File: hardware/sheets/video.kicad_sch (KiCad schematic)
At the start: 41 parts, among them J1 HDMI_A, J2 VGA HD15, M1 Core2350B (8MB PSRAM), U2 74LVC245A, U3 74LVC245A, U4 74LVC245A, U5 74LVC245A

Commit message: Passives: basic-library audit + 4x resistor-array pull consolidation
Audit: every discrete R/C value was already JLC basic except the ferrite
beads -- swapped to basic Murata BLM18PG121SN1D (C14709, 120R@100MHz,
same family/role). The 100uF electrolytic and buck inductor stay
extended (zero fee-free parts exist in those subcategories). Pruned the
orphaned 5V-era 47nF/330nF MAX3241 cap entries.

Pull consolidation: 65 discrete 10k/4.7k rail pulls across 8 sheets
collapse into 18 basic 4-element isolated arrays (4D03WGJ0103T5E /
4D03WGJ0472T5E, element k = pins k/9-k; new mxbus.r_pack4 helper).
Isolated elements let packs mix rails; every net keeps its exact rail
and semantics (verified element-by-element in the netlist). RC/divider/
series/I2C resistors stay discrete. Board 452 -> 406 components; also
de-risks the sole basic 10k 0603 line (0 stock at audit). Audit
recorded in jlcpcb-sourcing.md.

Co-Authored-By: Claude Fable 5 <noreply@anthropic.com>
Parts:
- removed JP1: VID_BASE, Connector_PinHeader_2.54mm:PinHeader_1x02_P2.54mm_Vertical, symbol Connector_Generic:Conn_01x02
- removed R33, R34, R35, R36: 10k, Resistor_SMD:R_0603_1608Metric, symbol Device:R
- added RN2: 10kx4, Resistor_SMD:R_Array_Convex_4x0603, symbol Device:R_Pack04
- JP1: renamed from R31; value 10k -> VID_BASE; footprint Resistor_SMD:R_0603_1608Metric -> Connector_PinHeader_2.54mm:PinHeader_1x02_P2.54mm_Vertical; symbol Device:R -> Connector_Generic:Conn_01x02; LCSC Part Num C25804 -> C2337
- RN1: renamed from R32; value 10k -> 10kx4; footprint Resistor_SMD:R_0603_1608Metric -> Resistor_SMD:R_Array_Convex_4x0603; symbol Device:R -> Device:R_Pack04; LCSC Part Num C25804 -> C29718
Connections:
- net 3V3_VID: now also RN1.5 (R4.2), RN1.6 (R3.2), RN1.7 (R2.2), RN1.8 (R1.2), RN2.8 (R1.2); no longer JP1.1
- net AOE_HI: now also RN1.4 (R4.1)
- net AOE_LO: now also RN1.2 (R2.1)
- net AOE_MID: now also RN1.3 (R3.1)
- net DDIR: now also RN2.2 (R2.1); no longer RN1.2
- net DOE: now also RN1.1 (R1.1)
- net GND: now also JP1.2 (Pin_2), RN2.7 (R2.2); no longer RN1.1
- net VID_BASE: now also JP1.1 (Pin_1), RN2.1 (R1.1); no longer JP1.2
- no-connect marks 30 -> 34

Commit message: Remove the on-board RTL8019AS NIC (tag full-board-with-nic preserves it)
Network sheet, symbols, and NIC-only parts.py bindings deleted; addr_decode
JP6->JP5 (DIS_VID); IRQ2 retired as an internal net like IRQ6/IRQ8 (still
reachable as EXT_IRQ2 from the expansion port). ERC stays 0/0.

Co-Authored-By: Claude Fable 5 <noreply@anthropic.com>
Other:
- note added: "SOFT CARD: ISA bus + power ONLY. Self-decodes 0xA0000-0xBFFFF and 3B4/3B5/3B8/3BA/3BF + 3D4/3D5/3D8/3D9/3DA from snooped A17-A19/A0-A9. No Y5, no link, no host RAM (design S8). Disable: addr_decode JP5 (DIS_VID high, firmware keeps all OEs off; enabled by default). JP1 = CGA (closed) / MDA (open) window set."
- note removed: "SOFT CARD: ISA bus + power ONLY. Self-decodes 0xA0000-0xBFFFF and 3B4/3B5/3B8/3BA/3BF + 3D4/3D5/3D8/3D9/3DA from snooped A17-A19/A0-A9. No Y5, no link, no host RAM (design S8). Disable: addr_decode JP6 (DIS_VID high, firmware keeps all OEs off; enabled by default). JP1 = CGA (closed) / MDA (open) window set."

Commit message: Expansion port: 50-pin header, port DMA channel, dev cards deleted
Two waves of the 2026-07-14/15 expansion-port rework (the first was
uncommitted): the IRQ-scan collapse to one '165 + '32 OR rank with
ISA-card DMA removed outright, then the port redesign that brings one
DMA channel back:

- isa_conn: 60-pin (2x30, PicoGUS-standard layout) -> 50-pin (2x25,
  project-private pinout; 50-way IDC is far easier to source). OSC and
  ~REFRESH dropped to fit (no on-board consumer / no DRAM refresh; the
  planned ISA backplane board re-creates both for period cards).
- Port DMA: EXT_DRQ rides the sidecar inbound '244 + U12 '165 spare D6
  lane (zero GPIO); ~EXT_DACK = GPIO47 (freed by ~REFRESH) out through
  the strobe '244. Separate nets from the internal PicoGUS pair, so a
  port card never sees the on-board acknowledge.
- DRQ1/~DACK1 renamed DRQ/~DACK (ch2/3 long retired); DRQ2/3 +
  ~DACK2/3 removed from the mxbus contract.
- card_video + card_isatest deleted (sheets, hardware/cards/,
  build_cards()); superseded by the backplane plan. History has them.
- Connector parts: IDE header -> shrouded 2x20 IDC box (C9138, keypin
  20 NC'd); expansion port -> 90-degree 2x25 female socket (C21262364);
  addr_decode's five disable jumpers folded into ONE fixed 2x5 block
  JP1 (C492422), positions JP1.1-JP1.5 = COM1/COM2/LPT/IDE/VID.

ERC 0/0, check_parts 0 problems; docs/notes updated throughout.

Co-Authored-By: Claude Fable 5 <noreply@anthropic.com>
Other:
- note added: "SOFT CARD: ISA bus + power ONLY. Self-decodes 0xA0000-0xBFFFF and 3B4/3B5/3B8/3BA/3BF + 3D4/3D5/3D8/3D9/3DA from snooped A17-A19/A0-A9. No Y5, no link, no host RAM (design S8). Disable: addr_decode JP1.5 (DIS_VID high, firmware keeps all OEs off; enabled by default). JP1 = CGA (closed) / MDA (open) window set."
- note removed: "SOFT CARD: ISA bus + power ONLY. Self-decodes 0xA0000-0xBFFFF and 3B4/3B5/3B8/3BA/3BF + 3D4/3D5/3D8/3D9/3DA from snooped A17-A19/A0-A9. No Y5, no link, no host RAM (design S8). Disable: addr_decode JP5 (DIS_VID high, firmware keeps all OEs off; enabled by default). JP1 = CGA (closed) / MDA (open) window set."

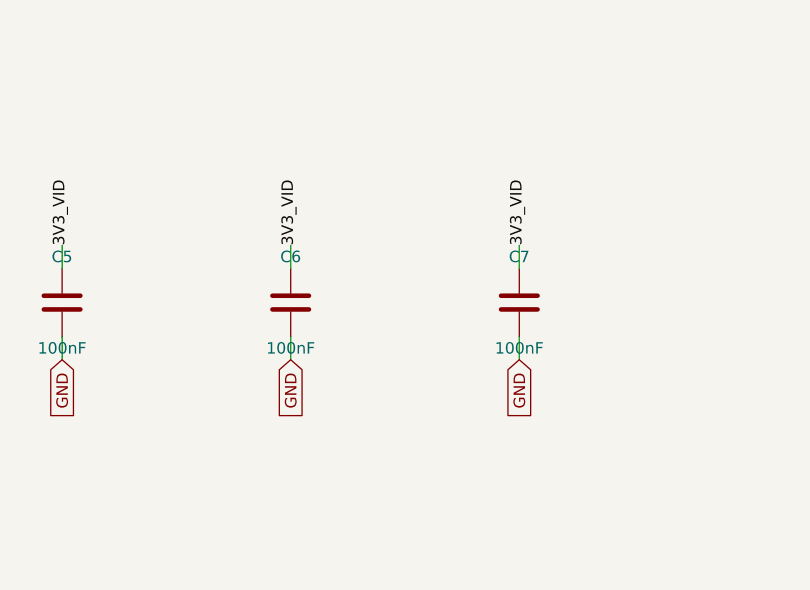
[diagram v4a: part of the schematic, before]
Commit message: Decoupling audit: drop video's 2 orphan caps, add 5 missing ones
Audit of every bypass cap against the ICs it decouples found one stale
remnant: video kept 6 3V3_VID caps for what are now 4 shifters (C6/C7
belonged to the deleted U6/U7). Removed them. All other sheets tally
one-per-IC.

Under-provisioned spots filled in the same pass: cpu_core C28 gives the
third surviving 5V part its own 100nF (V20/U10/U13 now 1 each), and
sidecar C8-C11 bring the port buffers to one cap per IC (U1-U4, U6-U9).

ERC 0/0; netlist verified (C128 on +5V, C1008-C1011 on +3V3).

Co-Authored-By: Claude Fable 5 <noreply@anthropic.com>
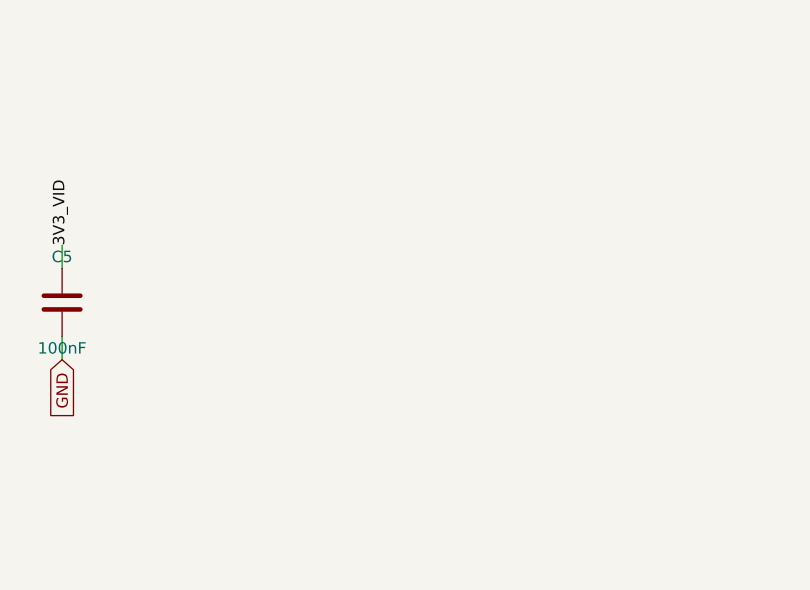
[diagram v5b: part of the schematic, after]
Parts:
- removed C7: 100nF, Capacitor_SMD:C_0603_1608Metric, symbol Device:C
- removed J2: VGA HD15, Connector_Dsub:DSUB-15-HD_Socket_Horizontal_P2.29x2.54mm_EdgePinOffset8.35mm_Housed_MountingHolesOffset10.89mm, symbol Connector_Generic:Conn_01x15
- removed R29: 100, Resistor_SMD:R_0603_1608Metric, symbol Device:R
- removed RN1: 10kx4, Resistor_SMD:R_Array_Convex_4x0603, symbol Device:R_Pack04
- added R20: 2k, Resistor_SMD:R_0603_1608Metric, symbol Device:R
- added R21: 1k, Resistor_SMD:R_0603_1608Metric, symbol Device:R
- J2: renamed from R28; value 100 -> VGA HD15; footprint Resistor_SMD:R_0603_1608Metric -> Connector_Dsub:DSUB-15-HD_Socket_Horizontal_P2.29x2.54mm_EdgePinOffset8.35mm_Housed_MountingHolesOffset10.89mm; symbol Device:R -> Connector_Generic:Conn_01x15; LCSC Part Num C22775 -> (none)
- R22: renamed from R20; value 2k -> 510; LCSC Part Num C22975 -> C23193
- R23: renamed from R21; value 1k -> 2k; LCSC Part Num C21190 -> C22975
- R24: renamed from R22; value 510 -> 1k; LCSC Part Num C23193 -> C21190
- R25: renamed from R23; value 2k -> 510; LCSC Part Num C22975 -> C23193
- R26: renamed from R24; value 1k -> 820; LCSC Part Num C21190 -> C23253
- R27: renamed from R25; value 510 -> 470; LCSC Part Num C23193 -> C23179
- R28: renamed from R26; value 820 -> 100; LCSC Part Num C23253 -> C22775
- R29: renamed from R27; value 470 -> 100; LCSC Part Num C23179 -> C22775
- RN1: renamed from C6; value 100nF -> 10kx4; footprint Capacitor_SMD:C_0603_1608Metric -> Resistor_SMD:R_Array_Convex_4x0603; symbol Device:C -> Device:R_Pack04; LCSC Part Num C14663 -> C29718
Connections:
- net 3V3_VID: now also RN1.5 (R4.2), RN1.6 (R3.2), RN1.7 (R2.2), RN1.8 (R1.2); no longer RN1.1
- net AOE_HI: now also RN1.4 (R4.1)
- net AOE_LO: now also RN1.2 (R2.1)
- net AOE_MID: now also RN1.3 (R3.1)
- net DOE: now also RN1.1 (R1.1)
- net GND: now also J2.10 (Pin_10), J2.5 (Pin_5), J2.6 (Pin_6), J2.7 (Pin_7), J2.8 (Pin_8); no longer RN1.2
- net HSYNC: now also R28.1; no longer J2.1
- net HSYNC_J: now also J2.13 (Pin_13), R28.2; no longer J2.2
- net VB0: now also R26.1; no longer R28.1
- net VB1: now also R27.1; no longer R29.1
- net VG0: now also R23.1; no longer R25.1
- net VG1: now also R24.1; no longer R26.1
- net VG2: now also R25.1; no longer R27.1
- net VGA_B: now also J2.3 (Pin_3), R26.2, R27.2; no longer R28.2, R29.2
- net VGA_G: now also J2.2 (Pin_2), R23.2, R24.2; no longer R26.2, R27.2
- net VGA_R: now also J2.1 (Pin_1), R20.2, R21.2; no longer R23.2, R24.2
- net VR0: now also R20.1; no longer R22.1
- net VR1: now also R21.1; no longer R23.1
- net VR2: now also R22.1; no longer R24.1
- net VSYNC: now also R29.1
- net VSYNC_J: now also J2.14 (Pin_14), R29.2
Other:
- moved on the sheet: R22, R23, R24, R25, R26, R27, R28, R29
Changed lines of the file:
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@@
 	(wire
 		(pts
-			(xy 177.8 270.51)
-			(xy 177.8 267.97)
-		)
-		(stroke
-			(width 0)
-			(type default)
-		)
-	)
-	(label "3V3_VID"
-		(at 177.8 267.97 90)
-		(effects
-			(font
-				(size 1.27 1.27)
-			)
-		)
-	)
-	(wire
-		(pts
-			(xy 177.8 278.13)
-			(xy 177.8 280.67)
-		)
-		(stroke
-			(width 0)
-			(type default)
-		)
-	)
-	(global_label "GND"
-		(shape input)
-		(at 177.8 280.67 270)
-		(effects
-			(font
-				(size 1.27 1.27)
-			)
-		)
-	)
-	(wire
-		(pts
-			(xy 203.2 270.51)
-			(xy 203.2 267.97)
-		)
-		(stroke
-			(width 0)
-			(type default)
-		)
-	)
-	(label "3V3_VID"
-		(at 203.2 267.97 90)
-		(effects
-			(font
-				(size 1.27 1.27)
-			)
-		)
-	)
-	(wire
-		(pts
-			(xy 203.2 278.13)
-			(xy 203.2 280.67)
-		)
-		(stroke
-			(width 0)
-			(type default)
-		)
-	)
-	(global_label "GND"
-		(shape input)
-		(at 203.2 280.67 270)
-		(effects
-			(font
-				(size 1.27 1.27)
-			)
-		)
-	)
-	(wire
-		(pts
 			(xy 43.18 292.1)
 			(xy 43.18 294.64)
@@
 					(unit 1)
 				)
-			)
-		)
-	)
-	(symbol
-		(lib_id "Device:C")
-		(at 177.8 274.32 0)
-		(unit 1)
-		(exclude_from_sim no)
-		(in_bom yes)
-		(on_board yes)
-		(dnp no)
-		(fields_autoplaced yes)
-		(property "Reference" "C6"
-			(at 177.8 269.24 0)
-			(effects
-				(font
-					(size 1.27 1.27)
-				)
-			)
-		)
-		(property "Value" "100nF"
-			(at 177.8 279.4 0)
-			(effects
-				(font
-					(size 1.27 1.27)
-				)
-			)
-		)
-		(property "Footprint" "Capacitor_SMD:C_0603_1608Metric"
-			(at 177.8 274.32 0)
-			(effects
-				(font
-					(size 1.27 1.27)
-				)
-				(hide yes)
-			)
-		)
-		(property "LCSC Part Num" "C14663"
-			(at 177.8 274.32 0)
-			(effects
-				(font
-					(size 1.27 1.27)
-				)
-				(hide yes)
-			)
-		)
-		(pin "1"
-		)
-		(pin "2"
-		)
-		(instances
-			(project "mini-xt"
-				(path "/26736c46-8b40-5460-874f-03596d17270c/3f5f8bf1-0374-5032-82b0-b1b8b2670099"
-					(reference "C406")
-					(unit 1)
-				)
-			)
-		)
-	)
-	(symbol
-		(lib_id "Device:C")
-		(at 203.2 274.32 0)
-		(unit 1)
-		(exclude_from_sim no)
-		(in_bom yes)
-		(on_board yes)
-		(dnp no)
-		(fields_autoplaced yes)
-		(property "Reference" "C7"
-			(at 203.2 269.24 0)
-			(effects
-				(font
-					(size 1.27 1.27)
-				)
-			)
-		)
-		(property "Value" "100nF"
-			(at 203.2 279.4 0)
-			(effects
-				(font
-					(size 1.27 1.27)
-				)
-			)
-		)
-		(property "Footprint" "Capacitor_SMD:C_0603_1608Metric"
-			(at 203.2 274.32 0)
-			(effects
-				(font
-					(size 1.27 1.27)
-				)
-				(hide yes)
-			)
-		)
-		(property "LCSC Part Num" "C14663"
-			(at 203.2 274.32 0)
-			(effects
-				(font
-					(size 1.27 1.27)
-				)
-				(hide yes)
-			)
-		)
-		(pin "1"
-		)
-		(pin "2"
-		)
-		(instances
-			(project "mini-xt"
-				(path "/26736c46-8b40-5460-874f-03596d17270c/3f5f8bf1-0374-5032-82b0-b1b8b2670099"
-					(reference "C407")
-					(unit 1)
-				)

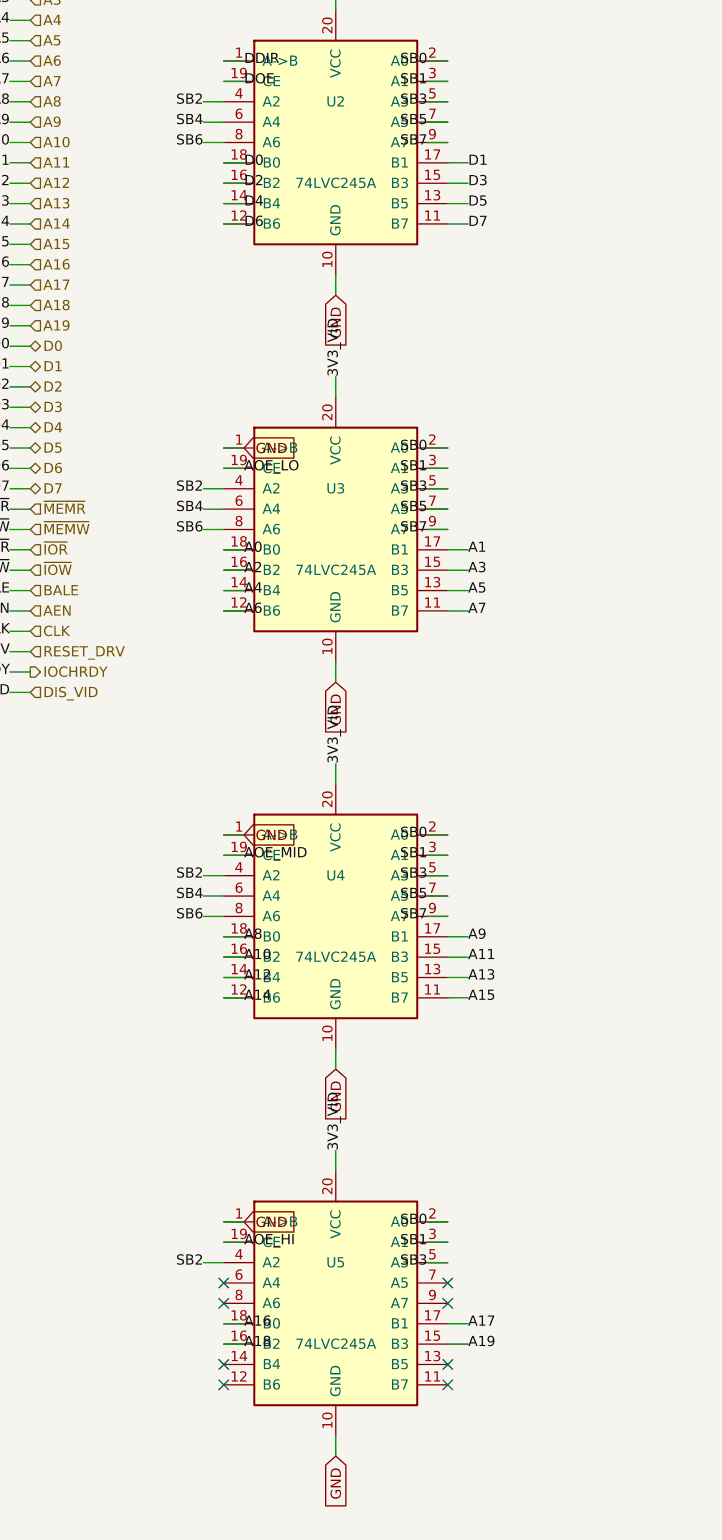
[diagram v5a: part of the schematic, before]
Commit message: KiCad 10 symbol support: read sharded .kicad_symdir libraries
The KiCad snap (which supplied the KiCad 9 monolithic .kicad_sym libs)
is gone; the KiCad 10 AppImage ships its libraries in the new sharded
format instead: <Lib>.kicad_symdir/ directories of one-symbol files.

- mxsch: lib_source() resolves a .kicad_sym path to the file or its
  .kicad_symdir sibling; SymbolLib.load() loads every file in a symdir
  (extends resolution runs after all files, since base and derived
  symbols live in separate files); kicad_symdir() falls back to
  ~/.local/share/kicad/<ver>/symbols (populated once from the AppImage)
- build/pins/gensym: route existence checks + copy_symbol through it
- power/supervisor: USB-C/USB-A shield pin renamed S1/5 -> SH in the
  KiCad 10 libs (the one real symbol-content change; still GND)
- selftest: netlist checker now tolerates KiCad 10's multiline netlist
  format (it silently found nothing since the CLI moved to 10)
- regenerate all sheets + mini-xt.kicad_sym from KiCad 10 sources: the
  churn is embedded-symbol format tokens only. Verified: ERC 0/0,
  before/after netlists have identical net->node sets (736 nets, only
  the shield-pin rename), double-build stays byte-identical, all seven
  custom symbols pin-identical after gensym regen.

Co-Authored-By: Claude Fable 5 <noreply@anthropic.com>
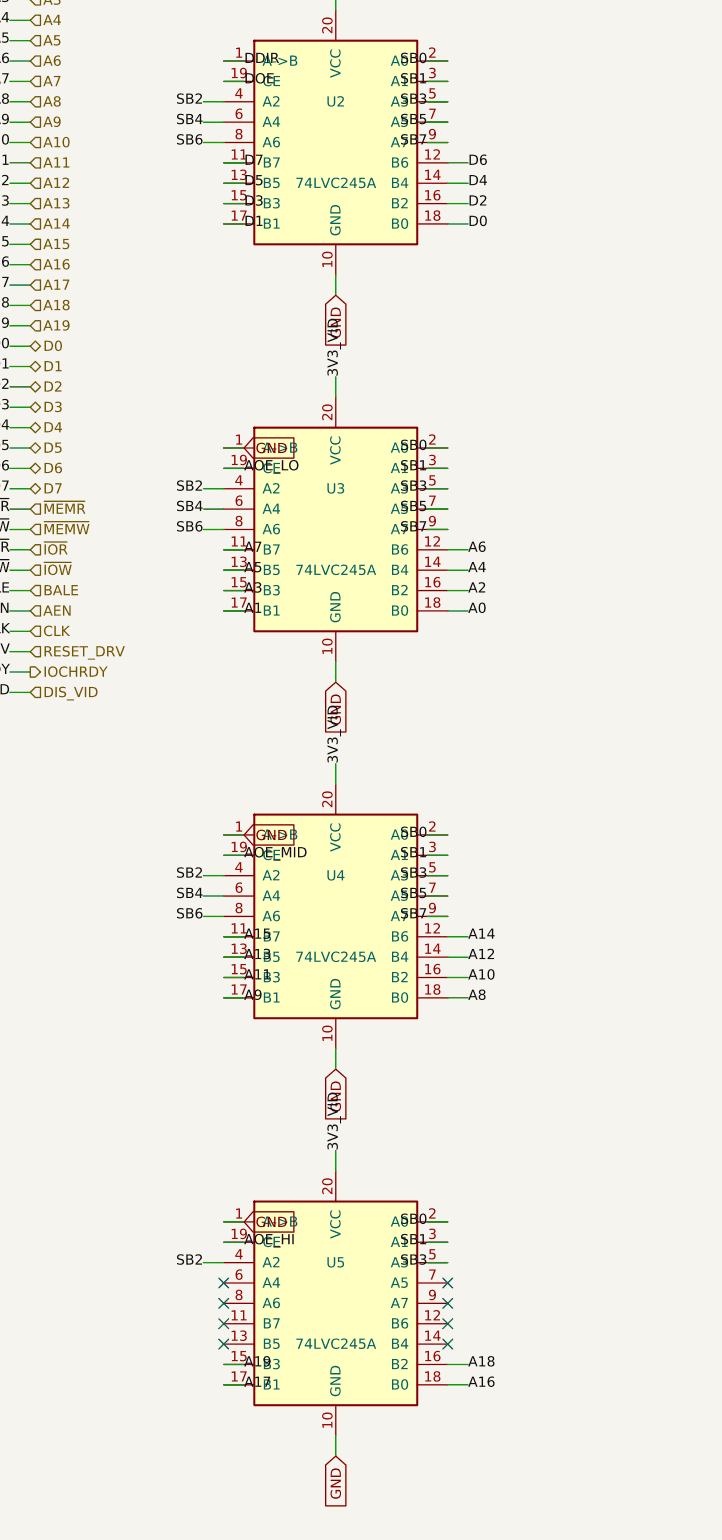
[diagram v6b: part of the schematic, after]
